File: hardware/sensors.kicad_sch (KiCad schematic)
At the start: 11 parts, among them U1 BME280, U2 ATGM336H

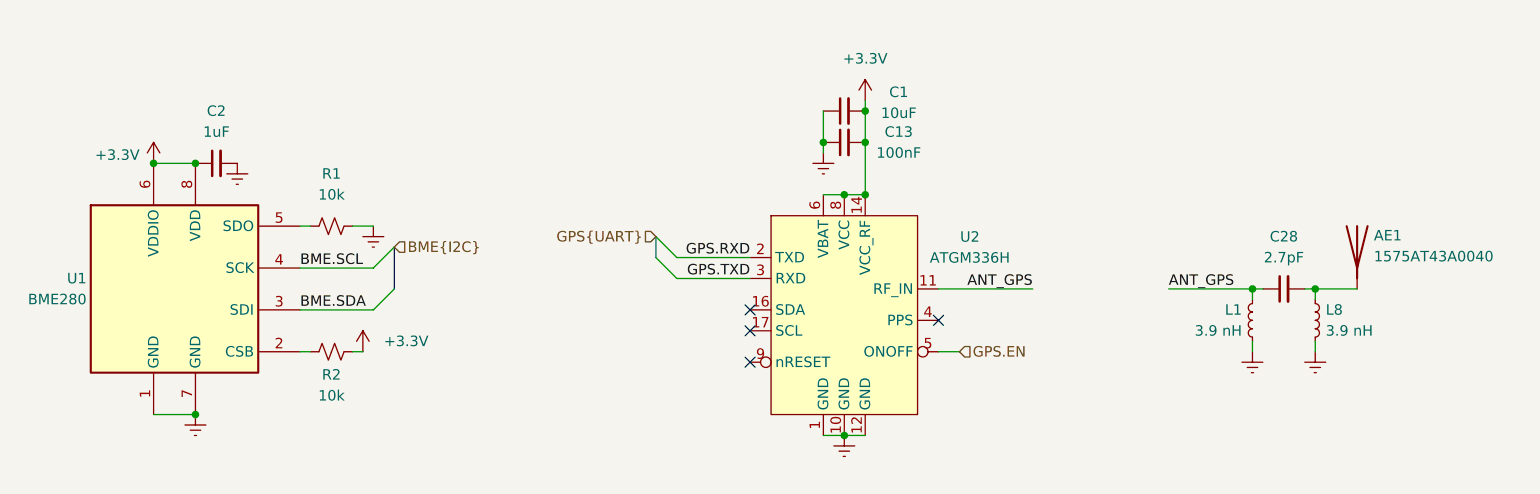
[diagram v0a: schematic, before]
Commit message: power path and bme280 fix
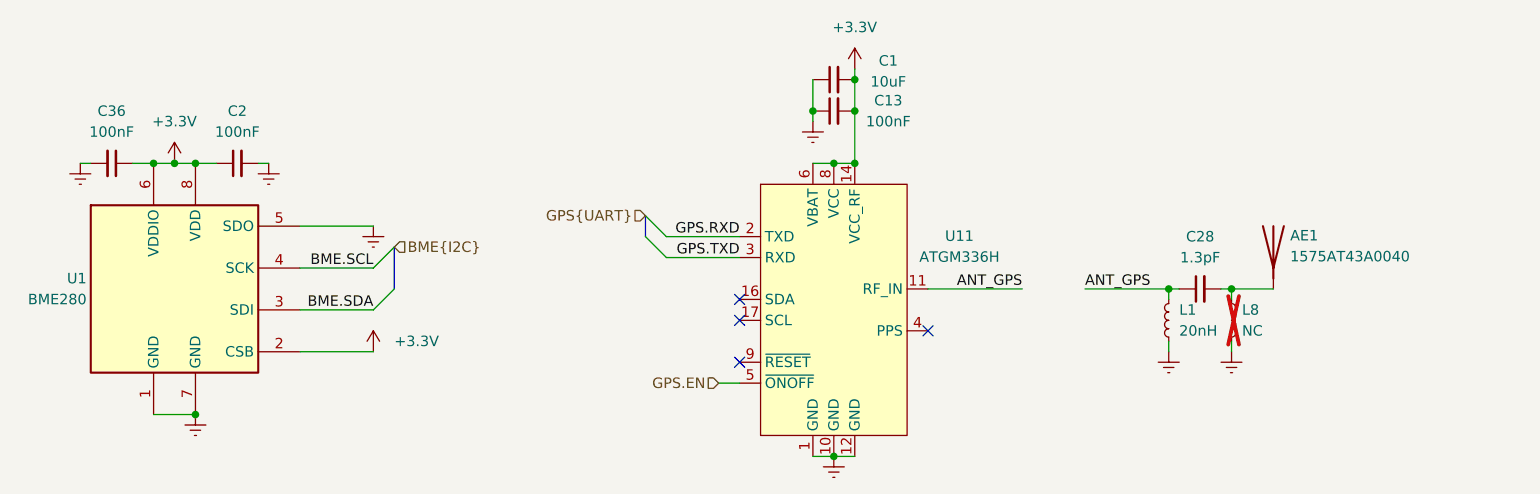
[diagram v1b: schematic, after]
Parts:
- removed R1, R2: 10k, Resistor_SMD:R_0402_1005Metric_Pad0.72x0.64mm_HandSolder, symbol Device:R_Small_US
- removed U2: ATGM336H, RF_GPS_Extended:ATGM336H, symbol RF_GPS_Extended:ATGM336H
- added C36: 100nF, Capacitor_SMD:C_0402_1005Metric_Pad0.74x0.62mm_HandSolder, symbol Device:C_Small
- added U11: ATGM336H, RF_GPS:ublox_MAX, symbol RF_GPS_Custom:ATGM336H
- C2: value 1uF -> 100nF
- C28: value 2.7pF -> 1.3pF
- L1: value 3.9 nH -> 20nH
- L8: value 3.9 nH -> NC; now not fitted
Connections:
- net +3.3V: now also U1.2 (CSB), C36.1, U11.14 (VCC_RF), U11.6 (VBAT), U11.8 (VCC)
- net ANT_GPS: now also U11.11 (RF_IN)
- net Earth: now also U1.5 (SDO), C36.2, U11.1 (GND), U11.10 (GND), U11.12 (GND)
- net GPS.EN: now also U11.5 (~{ONOFF})
- net GPS.RXD: now also U11.2 (TXD)
- net GPS.TXD: now also U11.3 (RXD)
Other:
- moved on the sheet: AE1, C1, C13, C2, C28, L1

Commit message: pcb rework -- layout subsections and rough floorplanning
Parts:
- AE1: footprint RF_Antenna_Extended:ANT_1575AT_JOT -> RF_Antenna:Johanson_2450AT43F0100_2400-2500Mhz
- C1, C13, C2, C28, C36: footprint Capacitor_SMD:C_0402_1005Metric_Pad0.74x0.62mm_HandSolder -> Capacitor_SMD:C_0402_1005Metric
- L1: footprint Inductor_SMD:L_0402_1005Metric_Pad0.77x0.64mm_HandSolder -> Capacitor_SMD:C_0402_1005Metric
- L8: footprint Inductor_SMD:L_0402_1005Metric_Pad0.77x0.64mm_HandSolder -> Inductor_SMD:L_0402_1005Metric
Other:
- note added: "GET ACTUAL FOOTPRINT"

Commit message: net class shenanigans
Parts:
- AE1, C1, C13, C2, C28, C36, L1, L8: KiLib_Generator (none) -> SMD_2terminal_chip_molded
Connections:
- net ANT_GPS: no longer names the net of C28.1, L1.2, U11.11 (RF_IN)
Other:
- moved on the sheet: AE1
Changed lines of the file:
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@@
 	(text "GET ACTUAL FOOTPRINT"
 		(exclude_from_sim no)
-		(at 236.22 97.028 0)
+		(at 229.997 94.996 0)
 		(effects
 			(font
@@
 	)
 	(junction
+		(at 219.71 106.68)
+		(diameter 0)
+		(color 0 0 0 0)
+	)
+	(junction
 		(at 173.99 91.44)
 		(diameter 0)
@@
 	)
 	(junction
-		(at 219.71 106.68)
-		(diameter 0)
-		(color 0 0 0 0)
-	)
-	(junction
 		(at 88.9 91.44)
 		(diameter 0)
@@
 	(wire
 		(pts
-			(xy 194.31 106.68) (xy 182.88 106.68)
+			(xy 182.88 106.68) (xy 212.09 106.68)
 		)
 		(stroke
@@
 	(wire
 		(pts
-			(xy 219.71 106.68) (xy 224.79 106.68)
-		)
-		(stroke
-			(width 0)
-			(type default)
-		)
-	)
-	(wire
-		(pts
 			(xy 168.91 91.44) (xy 171.45 91.44)
 		)
@@
 	(wire
 		(pts
+			(xy 219.71 106.68) (xy 236.22 106.68)
+		)
+		(stroke
+			(width 0)
+			(type default)
+		)
+	)
+	(wire
+		(pts
 			(xy 171.45 127) (xy 173.99 127)
 		)
@@
 		(pts
 			(xy 88.9 121.92) (xy 93.98 121.92)
-		)
-		(stroke
-			(width 0)
-			(type default)
-		)
-	)
-	(wire
-		(pts
-			(xy 201.93 106.68) (xy 212.09 106.68)
 		)
 		(stroke
@@
 		)
 	)
-	(label "ANT_GPS"
-		(at 201.93 106.68 0)
-		(effects
-			(font
-				(size 1.27 1.27)
-			)
-			(justify left bottom)
-		)
-	)
 	(label "BME.SDA"
 		(at 115.57 109.22 180)
-		(effects
-			(font
-				(size 1.27 1.27)
-			)
-			(justify right bottom)
-		)
-	)
-	(label "ANT_GPS"
-		(at 194.31 106.68 180)
 		(effects
 			(font
@@
 		(polyline
 			(pts
-				(xy 243.84 118.11) (xy 243.84 96.52) (xy 198.12 96.52) (xy 198.12 118.11)
+				(xy 210.82 100.33) (xy 210.82 96.52) (xy 198.12 96.52) (xy 198.12 100.33)
 			)
 			(stroke
@@
 		(length 2.54)
 		(shape round)
-		(at 220.98 96.52 0)
+		(at 203.2 106.68 0)
 		(fields_autoplaced yes)
 		(effects
@@
 		)
 		(property "Netclass" "50R"
-			(at 221.6785 93.98 0)
+			(at 203.8985 104.14 0)
 			(show_name no)
 			(do_not_autoplace no)
@@
 		)
 		(property "Component Class" ""
-			(at -40.64 8.89 0)
+			(at -58.42 19.05 0)
+			(show_name no)
+			(do_not_autoplace no)
+			(effects
+				(font
+					(size 1.27 1.27)
+					(italic yes)
+				)
+			)
+		)
+	)
+	(netclass_flag ""
+		(length 2.54)
+		(shape round)
+		(at 226.06 106.68 0)
+		(fields_autoplaced yes)
+		(effects
+			(font
+				(size 1.27 1.27)
+			)
+			(justify left bottom)
+		)
+		(property "Netclass" "50R"
+			(at 226.7585 104.14 0)
+			(show_name no)
+			(do_not_autoplace no)
+			(effects
+				(font
+					(size 1.27 1.27)
+				)
+				(justify left)
+			)
+		)
+		(property "Component Class" ""
+			(at -35.56 19.05 0)
 			(show_name no)
 			(do_not_autoplace no)
@@
 			)
 		)
+		(property "KiLib_Generator" "SMD_2terminal_chip_molded"
+			(at 219.71 110.49 0)
+			(hide yes)
+			(show_name no)
+			(do_not_autoplace no)
+			(effects
+				(font
+					(size 1.27 1.27)
+				)
+			)
+		)
 		(pin "1"
 		)
@@
 			)
 		)
+		(property "KiLib_Generator" "SMD_2terminal_chip_molded"
+			(at 99.06 91.44 0)
+			(hide yes)
+			(show_name no)
+			(do_not_autoplace no)
+			(effects
+				(font
+					(size 1.27 1.27)
+				)
+			)
+		)
 		(pin "1"
 		)
@@
 			)
 		)
+		(property "KiLib_Generator" "SMD_2terminal_chip_molded"
+			(at 171.45 81.28 0)
+			(hide yes)
+			(show_name no)
+			(do_not_autoplace no)
+			(effects
+				(font
+					(size 1.27 1.27)
+				)
+			)
+		)
 		(pin "1"
 		)
@@
 		(property "Mouser Price/Stock" ""
 			(at 215.9 106.68 90)
+			(hide yes)
+			(show_name no)
+			(do_not_autoplace no)
+			(effects
+				(font
+					(size 1.27 1.27)
+				)
+			)
+		)
+		(property "KiLib_Generator" "SMD_2terminal_chip_molded"
+			(at 215.9 106.68 0)
 			(hide yes)
 			(show_name no)
@@
 			)
 		)
+		(property "KiLib_Generator" "SMD_2terminal_chip_molded"
+			(at 83.82 91.44 0)
+			(hide yes)
+			(show_name no)
+			(do_not_autoplace no)
+			(effects
+				(font
+					(size 1.27 1.27)
+				)
+			)
+		)
 		(pin "1"
 		)
@@
 	(symbol
 		(lib_id "Device:Antenna")
-		(at 224.79 101.6 0)
+		(at 236.22 101.6 0)
 		(mirror y)
 		(unit 1)
@@
 		(dnp no)
 		(property "Reference" "AE1"
-			(at 226.822 100.2029 0)
+			(at 238.252 100.2029 0)
 			(show_name no)
 			(do_not_autoplace no)
@@
 		)
 		(property "Value" "1575AT43A0040"
-			(at 226.822 102.7429 0)
+			(at 238.252 102.7429 0)
 			(show_name no)
 			(do_not_autoplace no)
@@
 		)
 		(property "Footprint" "RF_Antenna:Johanson_2450AT43F0100_2400-2500Mhz"
-			(at 224.79 101.6 0)
+			(at 236.22 101.6 0)
 			(hide yes)
 			(show_name no)
@@
 		)
 		(property "Datasheet" ""
-			(at 224.79 101.6 0)
+			(at 236.22 101.6 0)
 			(hide yes)
 			(show_name no)
@@
 		)
 		(property "Description" "Antenna"
-			(at 224.79 101.6 0)
+			(at 236.22 101.6 0)
 			(hide yes)
 			(show_name no)
@@
 		)
 		(property "LCSC" "C239243"
-			(at 224.79 101.6 0)
+			(at 236.22 101.6 0)
 			(hide yes)
 			(show_name no)
@@
 		)
 		(property "Arrow Part Number" ""
-			(at 224.79 101.6 0)
+			(at 236.22 101.6 0)
 			(hide yes)
 			(show_name no)
@@
 		)
 		(property "Arrow Price/Stock" ""
-			(at 224.79 101.6 0)
+			(at 236.22 101.6 0)
 			(hide yes)
 			(show_name no)
@@
 		)
 		(property "Height" ""
-			(at 224.79 101.6 0)
+			(at 236.22 101.6 0)
 			(hide yes)
 			(show_name no)
@@
 		)
 		(property "Manufacturer_Name" ""
-			(at 224.79 101.6 0)
+			(at 236.22 101.6 0)
 			(hide yes)
 			(show_name no)
@@
 		)
 		(property "Manufacturer_Part_Number" ""
-			(at 224.79 101.6 0)
+			(at 236.22 101.6 0)
 			(hide yes)
 			(show_name no)
@@
 		)
 		(property "Mouser Part Number" ""
-			(at 224.79 101.6 0)
+			(at 236.22 101.6 0)
 			(hide yes)
 			(show_name no)
@@
 		)
 		(property "Mouser Price/Stock" ""
-			(at 224.79 101.6 0)
+			(at 236.22 101.6 0)
+			(hide yes)
+			(show_name no)
+			(do_not_autoplace no)
+			(effects
+				(font
+					(size 1.27 1.27)
+				)
+			)
+		)
+		(property "KiLib_Generator" "SMD_2terminal_chip_molded"
+			(at 236.22 101.6 0)
 			(hide yes)
 			(show_name no)
@@
 			)
 		)
+		(property "KiLib_Generator" "SMD_2terminal_chip_molded"
+			(at 171.45 85.09 0)
+			(hide yes)
+			(show_name no)
+			(do_not_autoplace no)
+			(effects
+				(font
+					(size 1.27 1.27)
+				)
+			)
+		)
 		(pin "1"
 		)
@@
 			(at 212.09 110.49 0)
 			(hide yes)
+			(show_name no)
+			(do_not_autoplace no)
+			(effects
+				(font
+					(size 1.27 1.27)
+				)
+			)
+		)
+		(property "KiLib_Generator" "SMD_2terminal_chip_molded"
+			(at 212.09 110.49 0)
+			(hide yes)

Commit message: fix footprints
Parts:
- AE1: footprint RF_Antenna:Johanson_2450AT43F0100_2400-2500Mhz -> RF_Antenna_Custom:ANT_1575AT_JOT
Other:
- note removed: "GET ACTUAL FOOTPRINT"
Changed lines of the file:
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@@
 	(generator_version "10.0")
 	(paper "A4")
-	(text "GET ACTUAL FOOTPRINT"
-		(exclude_from_sim no)
-		(at 229.997 94.996 0)
-		(effects
-			(font
-				(size 1.27 1.27)
-			)
-		)
-	)
 	(junction
 		(at 173.99 85.09)
@@
 			)
 		)
-		(property "Footprint" "RF_Antenna:Johanson_2450AT43F0100_2400-2500Mhz"
+		(property "Footprint" "RF_Antenna_Custom:ANT_1575AT_JOT"
 			(at 236.22 101.6 0)
 			(hide yes)
